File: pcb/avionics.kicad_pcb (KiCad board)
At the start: 2 copper layers, 0 parts

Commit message: start pcb routing!!
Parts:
- added ABI-042-RC601: BUZZER, avionics14:ABI-042-RC, F.Cu at (147.0, 48.0)
- added C101: 10µ, avionics14:0603, F.Cu at (169.4, 121.0)
- added C102: 100n, avionics14:0603, F.Cu at (164.9, 115.6)
- added C103: 100n, avionics14:0603, F.Cu at (160.4, 121.0)
- added C104: 1µ, avionics14:0603, F.Cu at (153.5, 123.0)
- added C105: 100n, avionics14:0603, F.Cu at (153.5, 128.4)
- added C106: 15p, avionics14:0603, F.Cu at (164.9, 121.0)
- added C107: 15p, avionics14:0603, F.Cu at (169.4, 115.6)
- added C108: 10n, avionics14:0603, F.Cu at (158.0, 126.4)
- added C109: 100n, avionics14:0603, F.Cu at (150.8, 133.8)
- added C110: 100n, avionics14:0603, F.Cu at (162.5, 126.4)
- added C111: 2µ2, avionics14:0603, F.Cu at (155.3, 133.8)
- added C112: 100n, avionics14:0603, F.Cu at (150.8, 139.2)
- added C113: 2µ2, avionics14:0603, F.Cu at (160.4, 115.6)
- added C114: 100n, avionics14:0603, F.Cu at (159.8, 131.8)
- added C115: 2µ2, avionics14:0603, F.Cu at (167.1, 126.4)
- added C116: 1n, avionics14:0603, F.Cu at (155.3, 139.2)
- added C117: 2µ2, avionics14:0603, F.Cu at (159.8, 137.2)
- added C201: 100n, avionics14:0603, F.Cu at (69.0, 76.0)
- added C202: 100n, avionics14:0603, F.Cu at (69.0, 73.0)
- added C203: 100n, avionics14:0603, F.Cu at (66.0, 56.0)
- added C204: 100n, avionics14:0603, F.Cu at (70.0, 51.0)
- added C401: 100nF, avionics14:0603, F.Cu at (89.0, 50.0)
- added C701: 10µ, avionics14:0603, F.Cu at (149.2, 159.0)
- added C702: 10µ, avionics14:0603, F.Cu at (153.7, 153.6)
- added C703: 100n, avionics14:0603, F.Cu at (143.3, 164.4)
- added C704: 100n, avionics14:0603, F.Cu at (147.8, 164.4)
- added C705: 100n, avionics14:0603, F.Cu at (138.8, 169.8)
- added C706: 10n, avionics14:0603, F.Cu at (131.0, 171.8)
- added C707: 470n, avionics14:0603, F.Cu at (144.7, 159.0)
- added C708: 100n, avionics14:0603, F.Cu at (149.2, 153.6)
- added C709: 100n, avionics14:0603, F.Cu at (138.8, 164.4)
- added C710: 4µ7, avionics14:0603, F.Cu at (134.3, 166.4)
- added C711: 220n, avionics14:0603, F.Cu at (144.7, 153.6)
- added D501: ESD8V0R1B-02LS, avionics14:TSSLP-2-1, F.Cu at (177.5, 67.0)
- added D502: ESD8V0R1B-02LS, avionics14:TSSLP-2-1, F.Cu at (177.5, 60.0)
- added D503: ESD8V0R1B-02LS, avionics14:TSSLP-2-1, F.Cu at (177.5, 53.0)
- added D504: ESD8V0R1B-02LS, avionics14:TSSLP-2-1, F.Cu at (162.0, 48.0)
- added D601: LED_GREEN, avionics14:0603_LED, F.Cu at (124.0, 58.0)
- added D602: LED_RED, avionics14:0603_LED, F.Cu at (121.0, 58.0)
- added D603: LED_GREEN, avionics14:0603_LED, F.Cu at (112.0, 58.0)
- added D604: LED_RED, avionics14:0603_LED, F.Cu at (109.0, 58.0)
- added D605: LED_GREEN, avionics14:0603_LED, F.Cu at (118.0, 58.0)
- added D606: LED_RED, avionics14:0603_LED, F.Cu at (115.0, 58.0)
- added IC101: STM32F405VGT, avionics14:LQFP100, F.Cu at (109.0, 78.0)
- added IC102: ADP3335, avionics14:MSOP8, F.Cu at (182.0, 83.0)
- added IC701: ADXL345, avionics14:ADXL3x5, F.Cu at (130.0, 69.0)
- added IC702: L3G4200D, avionics14:L3G4200D, F.Cu at (102.0, 67.0)
- added IC703: MS5611-01BA03, avionics14:MS5611-01BA, F.Cu at (124.0, 51.0)
- added IC704: HMC5883L, avionics14:HMC5883L, F.Cu at (131.0, 59.0)
- added P101: CONN_01X02, avionics14:S02B-PASK-2, F.Cu at (179.0, 73.0)
- added P102: CONN_01X04, avionics14:S04B-PASK-2, F.Cu at (179.0, 80.0)
- added P103: SWD, avionics14:FTSH-105-01-F-D-K, F.Cu at (106.0, 48.0)
- added P201: SMA, avionics14:SMA-142-0701-801, F.Cu at (51.0, 80.0)
- added P202: SMA, avionics14:SMA-142-0701-801, F.Cu at (51.0, 49.0)
- added P501: CONN_01X02, avionics14:S02B-PASK-2, F.Cu at (179.0, 66.0)
- added P502: CONN_01X02, avionics14:S02B-PASK-2, F.Cu at (179.0, 59.0)
- added P503: CONN_01X02, avionics14:S02B-PASK-2, F.Cu at (179.0, 52.0)
- added P504: CONN_01X02, avionics14:S02B-PASK-2, F.Cu at (179.0, 45.0)
- added Q501: IRF7910, avionics14:SO-8, F.Cu at (147.8, 67.5)
- added Q502: FDN304P, avionics14:SOT23, F.Cu at (172.0, 65.8)
- added Q503: FDN304P, avionics14:SOT23, F.Cu at (169.0, 53.0)
- added Q504: IRF7910, avionics14:SO-8, F.Cu at (139.8, 59.0)
- added Q505: FDN304P, avionics14:SOT23, F.Cu at (169.0, 60.0)
- added Q506: FDN304P, avionics14:SOT23, F.Cu at (170.0, 45.0)
- added Q601: IRF7910, avionics14:SO-8, F.Cu at (137.0, 48.0)
- added R101: 100, avionics14:0603, F.Cu at (164.3, 131.8)
- added R201: 10K, avionics14:0603, F.Cu at (76.0, 77.0)
- added R202: 2.2K, avionics14:0603, F.Cu at (64.0, 73.0)
- added R203: 2.2K, avionics14:0603, F.Cu at (64.0, 76.0)
- added R401: 51k, avionics14:0603, F.Cu at (100.0, 49.6)
- added R402: 51k, avionics14:0603, F.Cu at (90.2, 60.4)
- added R403: 51k, avionics14:0603, F.Cu at (95.0, 52.0)
- added R404: 51k, avionics14:0603, F.Cu at (90.2, 55.0)
- added R501: 1k, avionics14:0603, F.Cu at (172.2, 69.8)
- added R502: 1k, avionics14:0603, F.Cu at (163.0, 56.0)
- added R503: 100k, avionics14:0603, F.Cu at (174.5, 68.8)
- added R504: 100k, avionics14:0603, F.Cu at (173.0, 56.0)
- added R505: 100k, avionics14:0603, F.Cu at (169.2, 65.8)
- added R506: 100k, avionics14:0603, F.Cu at (159.0, 54.0)
- added R507: 51k, avionics14:0603, F.Cu at (172.2, 68.2)
- added R508: 51k, avionics14:0603, F.Cu at (158.0, 51.0)
- added R509: 51k, avionics14:0603, F.Cu at (174.5, 65.0)
- added R510: 51k, avionics14:0603, F.Cu at (165.0, 54.0)
- added R511: 1k, avionics14:0603, F.Cu at (165.0, 61.0)
- added R512: 1k, avionics14:0603, F.Cu at (157.0, 44.0)
- added R513: 100k, avionics14:0603, F.Cu at (174.0, 61.0)
- added R514: 100k, avionics14:0603, F.Cu at (173.0, 49.0)
- added R515: 100k, avionics14:0603, F.Cu at (154.0, 60.0)
- added R516: 100k, avionics14:0603, F.Cu at (161.0, 45.0)
- added R517: 51k, avionics14:0603, F.Cu at (172.0, 59.0)
- added R518: 51k, avionics14:0603, F.Cu at (173.0, 46.0)
- added R519: 51k, avionics14:0603, F.Cu at (157.0, 60.0)
- added R520: 51k, avionics14:0603, F.Cu at (164.0, 45.0)
- added R601: 130, avionics14:0603, F.Cu at (124.0, 60.0)
- added R602: 150, avionics14:0603, F.Cu at (121.0, 60.0)
- added R603: 130, avionics14:0603, F.Cu at (112.0, 60.0)
- added R604: 150, avionics14:0603, F.Cu at (109.0, 60.0)
- added R605: 130, avionics14:0603, F.Cu at (118.0, 60.0)
- added R606: 150, avionics14:0603, F.Cu at (115.0, 60.0)
- added R607: 510, avionics14:0603, F.Cu at (136.0, 42.0)
- added R701: 10k, avionics14:0603, F.Cu at (153.7, 159.0)
- added R702: 10k, avionics14:0603, F.Cu at (99.0, 68.0)
- added R703: 10k, avionics14:0603, F.Cu at (143.3, 169.8)
- added R704: 10k, avionics14:0603, F.Cu at (126.5, 169.8)
- added R705: 10k, avionics14:0603, F.Cu at (147.8, 169.8)
- added R706: R, avionics14:0603, F.Cu at (134.3, 161.0)
- added R707: 10k, avionics14:0603, F.Cu at (140.2, 159.0)
- added U201: A2235-H, avionics14:a2235-h, F.Cu at (56.0, 84.0)
- added U202: RFM69W, avionics14:rfm69w, F.Cu at (79.0, 45.0)
- added U401: MICROSD_HOLDER, avionics14:MEM2051, F.Cu at (118.0, 99.1)
- added X101: 8M, avionics14:XTAL50x32, F.Cu at (113.0, 83.0)
- added ~401: MICROSD_HOLDER, avionics14:MEM2051, F.Cu at (103.0, 58.0)
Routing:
- net Net-(D501-Pad1): track 0.00 -> 10.5 mm
- net GND: track 0.00 -> 6.35 mm
- net +BATT: track 0.00 -> 3.61 mm
- net Net-(Q501-Pad7): track 0.00 -> 1.84 mm
- net Net-(Q501-Pad2): track 0.00 -> 1.64 mm
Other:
- board outline added: 140 x 48 mm
- net class Default: clearance 0.254 -> 0.15; trace_width 0.254 -> 0.2; via_dia 0.889 -> 1.4; via_drill 0.635 -> 0.8
- rule trace_clearance: 0.254 -> 0.15
- rule trace_min: 0.254 -> 0.15
- rule via_min_drill: 0.508 -> 0.6
- rule via_min_size: 0.889 -> 1.2

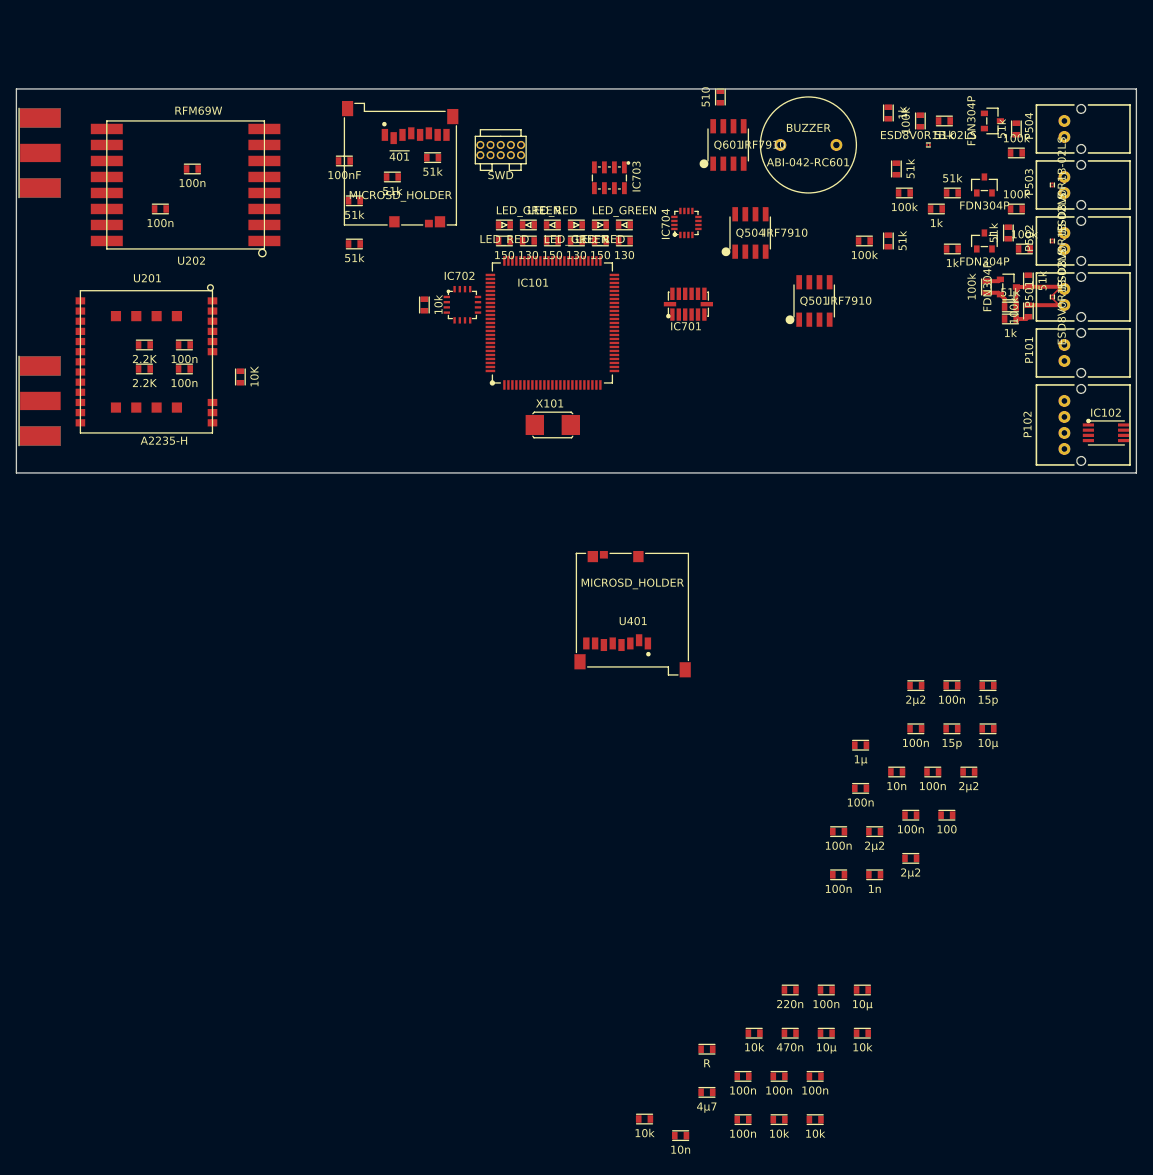
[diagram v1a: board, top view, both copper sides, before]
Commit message: swap GPS module to uBlox
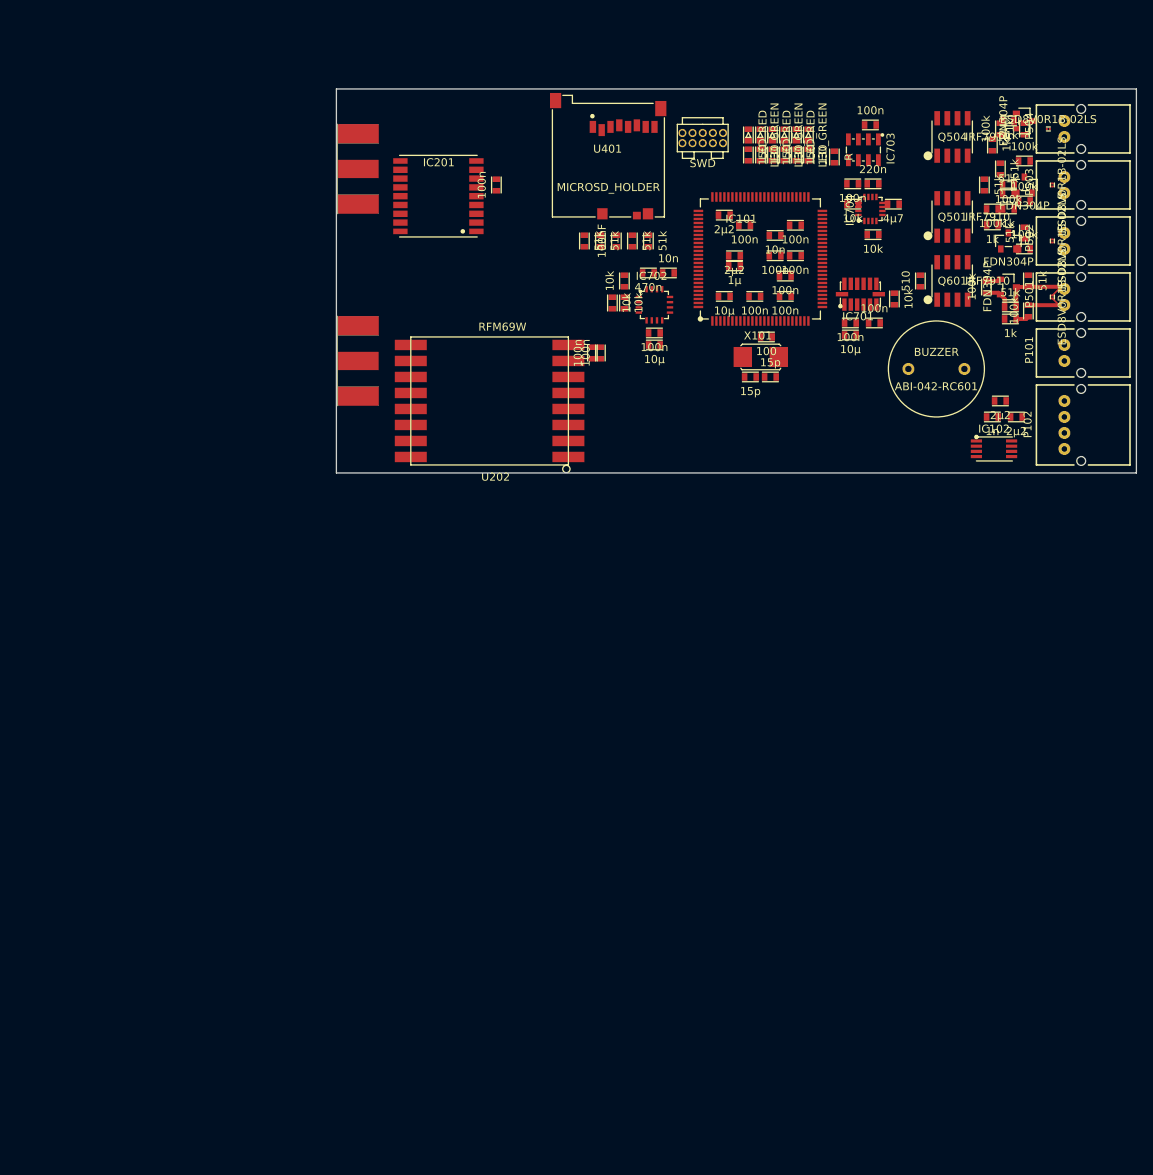
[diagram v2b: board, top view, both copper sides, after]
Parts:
- removed C202: 100n, avionics14:0603
- removed R201: 10K, avionics14:0603
- removed R202, R203: 2.2K, avionics14:0603
- removed U201: A2235-H, avionics14:a2235-h
- removed ~401: MICROSD_HOLDER, avionics14:MEM2051
- added IC201: MAX-7Q, avionics14:MAX-7Q, F.Cu at (96.0, 50.0)
- moved R705 114.5 mm to (152.5, 55.4)
- moved C710 113.4 mm to (157.6, 55.4)
- moved R706 112.7 mm to (150.2, 49.5), turned to 90 degrees
- moved C709 112.4 mm to (152.5, 52.9)
- moved C708 108.3 mm to (154.8, 45.5), turned to 180 degrees
- moved C706 107.8 mm to (129.5, 64.0), turned to 180 degrees
- moved R704 104.8 mm to (124.0, 65.0), turned to 270 degrees
- moved R703 103.6 mm to (157.8, 67.2), turned to 90 degrees
- moved C711 101.3 mm to (155.1, 52.9), turned to 180 degrees
- moved C705 100.9 mm to (155.2, 70.2), turned to 180 degrees
- moved R707 100.9 mm to (155.1, 59.2)
- moved C707 96.7 mm to (127.0, 64.0)
- moved R701 96.0 mm to (124.0, 67.8), turned to 90 degrees
- moved C704 95.1 mm to (127.8, 71.5)
- moved C703 94.6 mm to (152.2, 70.2)
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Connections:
- IC101 pad 70: /Radio/GPS_ON/OFF -> /Radio/GPS_nRST
- IC101 pad 71: /Radio/GPS_nRST -> Net-(IC101-Pad71)
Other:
- board size 140 x 48 mm -> 100 x 48 mm

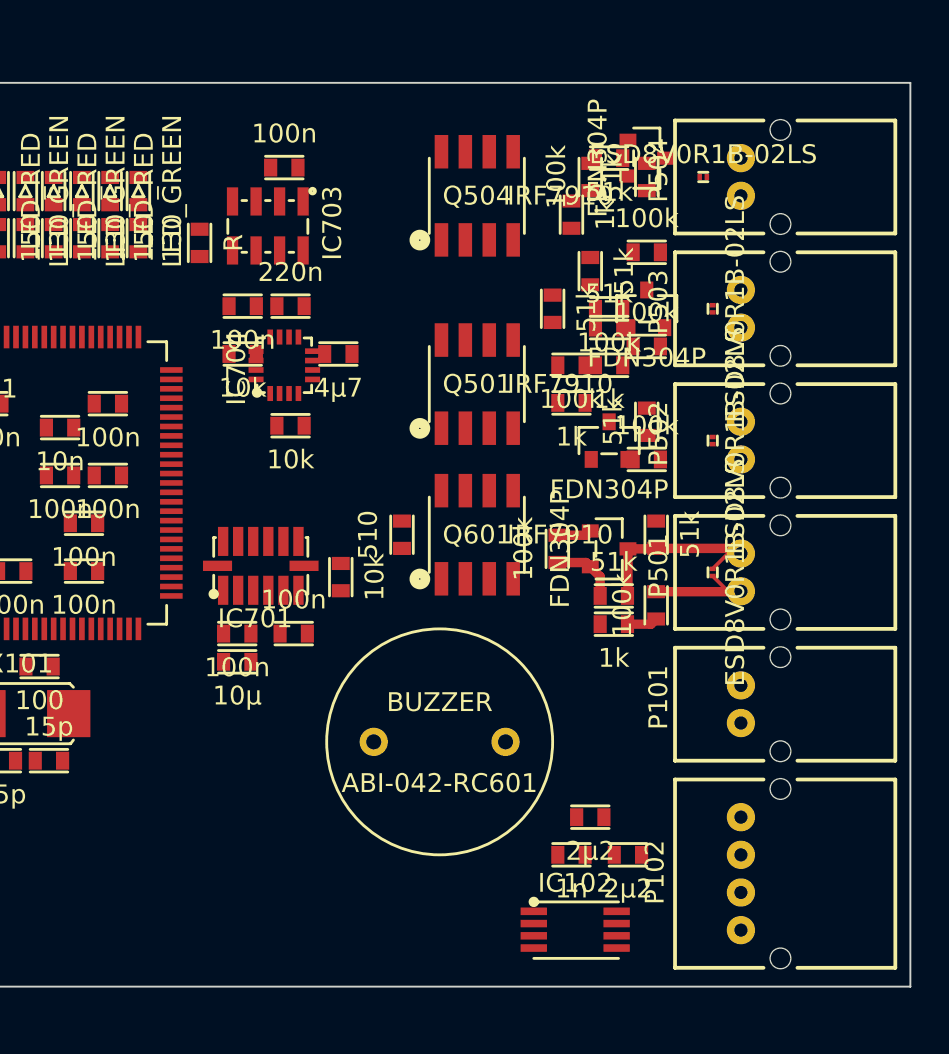
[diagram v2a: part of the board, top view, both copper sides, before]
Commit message: Tried to do a bit of routing. Couldn't really make any progress. Probably have to use thinner tracks, and might have to hop across the layers.
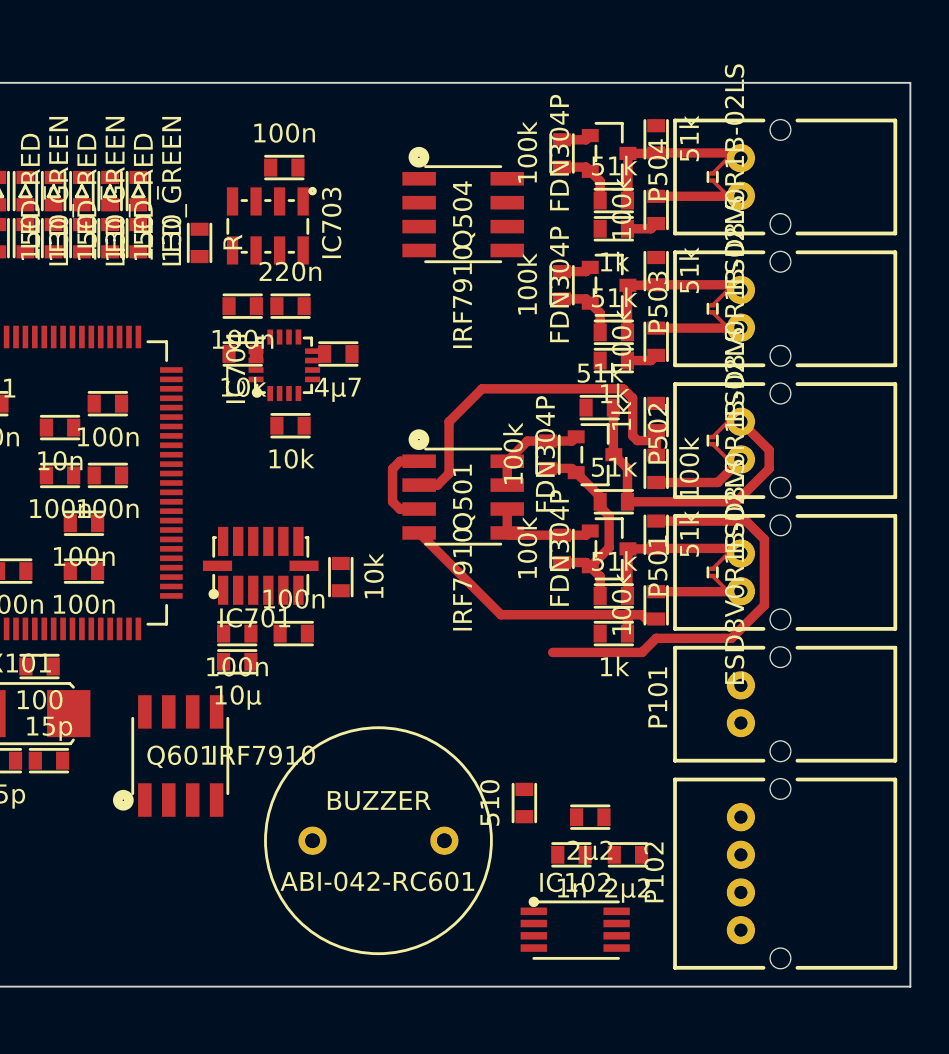
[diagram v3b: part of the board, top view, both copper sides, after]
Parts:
- moved Q601 19.7 mm to (149.2, 76.8)
- moved R607 15.7 mm to (167.5, 79.2)
- moved ABI-042-RC601 6.17 mm to (159.8, 81.2)
- moved Q501 6.05 mm to (164.2, 63.0), turned to 270 degrees
- moved R519 5.81 mm to (171.5, 58.2), turned to 180 degrees
- moved R515 4.91 mm to (168.8, 60.8), turned to 270 degrees
- moved R517 4.60 mm to (172.2, 63.2), turned to 180 degrees
- moved R511 4.56 mm to (174.5, 58.8), turned to 270 degrees
- moved R510 3.91 mm to (174.5, 51.0), turned to 90 degrees
- moved R508 3.48 mm to (172.2, 54.2), turned to 180 degrees
- moved R506 2.80 mm to (169.5, 51.8), turned to 270 degrees
- moved R520 2.69 mm to (174.5, 44.0), turned to 90 degrees
- moved R512 2.37 mm to (172.2, 48.8), turned to 0 degrees
- moved Q503 2.36 mm to (172.0, 51.8), turned to 270 degrees
- moved R514 2.30 mm to (174.5, 47.8), turned to 270 degrees
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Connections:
- Q502 pad 1: Net-(Q501-Pad7) -> Net-(Q501-Pad5)
- Q503 pad 1: Net-(Q501-Pad5) -> Net-(Q503-Pad1)
- Q503 pad 3: Net-(D502-Pad1) -> Net-(D503-Pad1)
- Q504 pad 5: Net-(Q504-Pad5) -> Net-(Q503-Pad1)
- Q504 pad 6: Net-(Q504-Pad5) -> Net-(Q503-Pad1)
- Q505 pad 1: Net-(Q504-Pad7) -> Net-(Q501-Pad7)
- Q505 pad 3: Net-(D503-Pad1) -> Net-(D502-Pad1)
- Q506 pad 1: Net-(Q504-Pad5) -> Net-(Q504-Pad7)
- R501 pad 2: Net-(Q501-Pad2) -> Net-(Q501-Pad4)
- R502 pad 2: Net-(Q501-Pad4) -> Net-(Q504-Pad4)
- R503 pad 2: Net-(Q501-Pad2) -> Net-(Q501-Pad4)
- R504 pad 2: Net-(Q501-Pad4) -> Net-(Q504-Pad4)
- R505 pad 1: Net-(Q501-Pad7) -> Net-(Q501-Pad5)
- R506 pad 1: Net-(Q501-Pad5) -> Net-(Q503-Pad1)
- R508 pad 1: Net-(D502-Pad1) -> Net-(D503-Pad1)
- R510 pad 1: Net-(D502-Pad1) -> Net-(D503-Pad1)
- R511 pad 2: Net-(Q504-Pad2) -> Net-(Q501-Pad2)
- R512 pad 2: Net-(Q504-Pad4) -> Net-(Q504-Pad2)
- R513 pad 2: Net-(Q504-Pad2) -> Net-(Q501-Pad2)
- R514 pad 2: Net-(Q504-Pad4) -> Net-(Q504-Pad2)
- R515 pad 1: Net-(Q504-Pad7) -> Net-(Q501-Pad7)
- R516 pad 1: Net-(Q504-Pad5) -> Net-(Q504-Pad7)
- R517 pad 1: Net-(D503-Pad1) -> Net-(D502-Pad1)
- R519 pad 1: Net-(D503-Pad1) -> Net-(D502-Pad1)
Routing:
- net GND: track 6.35 -> 30.8 mm
- net /Datalogging & Pyros/~PY1_CHK: track 0.00 -> 21.9 mm
- net Net-(D502-Pad1): track 0.00 -> 18.9 mm
- net Net-(Q501-Pad2): track 1.64 -> 19.9 mm
- net Net-(Q501-Pad4): track 0.00 -> 16.0 mm
- net +BATT: track 3.61 -> 17.8 mm
- net Net-(D504-Pad1): track 0.00 -> 10.5 mm
- net Net-(D503-Pad1): track 0.00 -> 10.5 mm
- net Net-(Q501-Pad5): track 0.00 -> 5.82 mm
- net Net-(Q501-Pad7): track 1.84 -> 5.47 mm
- net Net-(Q504-Pad4): track 0.00 -> 1.64 mm
- net Net-(Q504-Pad2): track 0.00 -> 1.64 mm
- net Net-(Q504-Pad7): track 0.00 -> 1.59 mm
- net Net-(Q503-Pad1): track 0.00 -> 1.59 mm

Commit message: continue pyro routing
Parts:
- D501, D502, D503, D504: value ESD8V0R1B-02LS -> CGA0402MLC-12G; footprint avionics14:TSSLP-2-1 -> avionics14:R0402
- moved IC102 13.5 mm to (168.4, 71.5)
- moved C117 11.2 mm to (166.4, 73.0), turned to 270 degrees
- moved Q601 10.1 mm to (158.4, 81.0), turned to 180 degrees
- moved R706 9.75 mm to (159.0, 45.2)
- moved C115 9.32 mm to (174.6, 71.4), turned to 90 degrees
- moved R511 8.11 mm to (166.4, 59.2), turned to 0 degrees
- moved R501 7.96 mm to (165.4, 66.2)
- moved ABI-042-RC601 7.86 mm to (167.6, 81.6), turned to 270 degrees
- moved R502 7.63 mm to (165.4, 52.4)
- moved C116 7.05 mm to (170.8, 75.0)
- moved R503 6.98 mm to (168.0, 66.2), turned to 180 degrees
- moved R504 6.91 mm to (168.0, 52.4), turned to 180 degrees
- moved R512 6.89 mm to (166.6, 44.8)
- moved R607 6.57 mm to (173.8, 77.4), turned to 0 degrees
- moved R510 6.41 mm to (169.2, 54.6), turned to 180 degrees
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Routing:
- net +BATT: track 17.8 -> 121.4 mm
- net GND: track 30.8 -> 8.87 mm
- net /Datalogging & Pyros/~PY1_CHK: track 21.9 -> 0.00 mm
- net Net-(Q501-Pad2): track 19.9 -> 5.94 mm
- net Net-(Q501-Pad4): track 16.0 -> 3.51 mm
- net +3V3: track 0.00 -> 10.9 mm
- net Net-(ABI-042-RC601-Pad2): track 0.00 -> 9.29 mm
- net Net-(D501-Pad1): track 10.5 -> 18.9 mm
- net Net-(D502-Pad1): track 18.9 -> 11.0 mm
- net Net-(D503-Pad1): track 10.5 -> 18.1 mm
- net Net-(ABI-042-RC601-Pad1): track 0.00 -> 5.76 mm
- net Net-(Q504-Pad7): track 1.59 -> 6.60 mm
- net Net-(Q504-Pad2): track 1.64 -> 6.31 mm
- net Net-(Q503-Pad1): track 1.59 -> 5.77 mm
- net Net-(C116-Pad2): track 0.00 -> 2.74 mm
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- added copper zone on B.Cu, net GND
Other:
- net class Default: via_dia 1.4 -> 1; via_drill 0.8 -> 0.6
- rule trace_min: 0.15 -> 0.2
- rule via_min_size: 1.2 -> 1
